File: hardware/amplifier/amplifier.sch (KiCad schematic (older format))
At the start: 39 parts, among them IC3 AD8331, IC4 ISL55210, P2 OUT, X1 IN

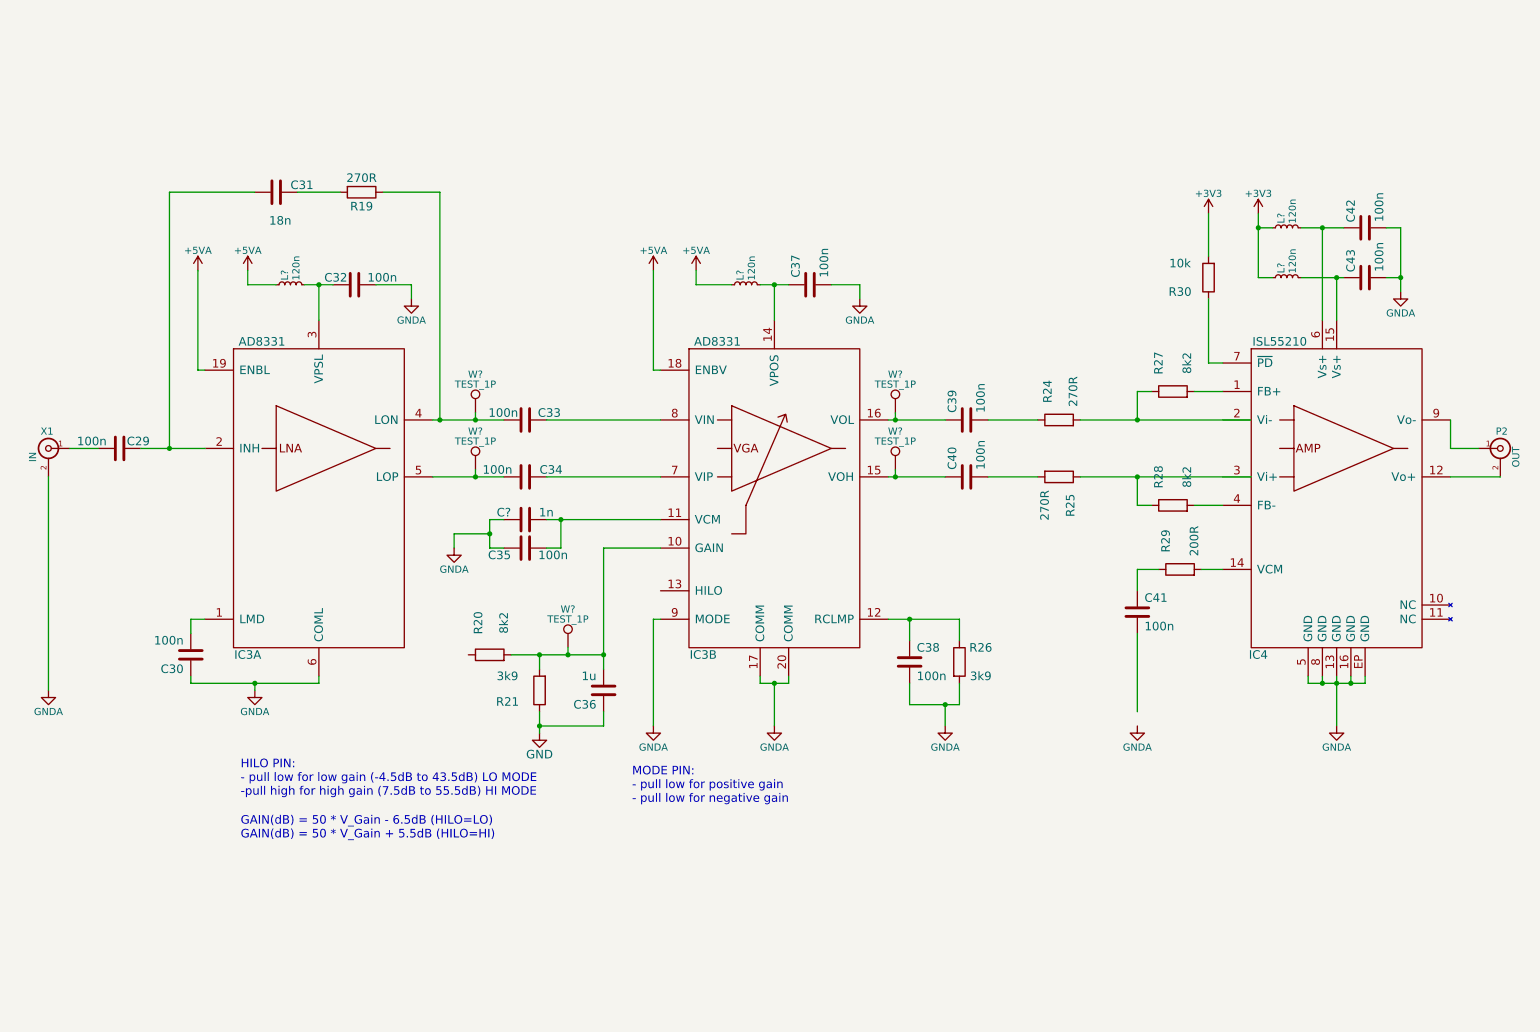
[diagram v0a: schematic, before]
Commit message: Worked on amp schema; nearly done; ISL55210 needs review as well as output termination
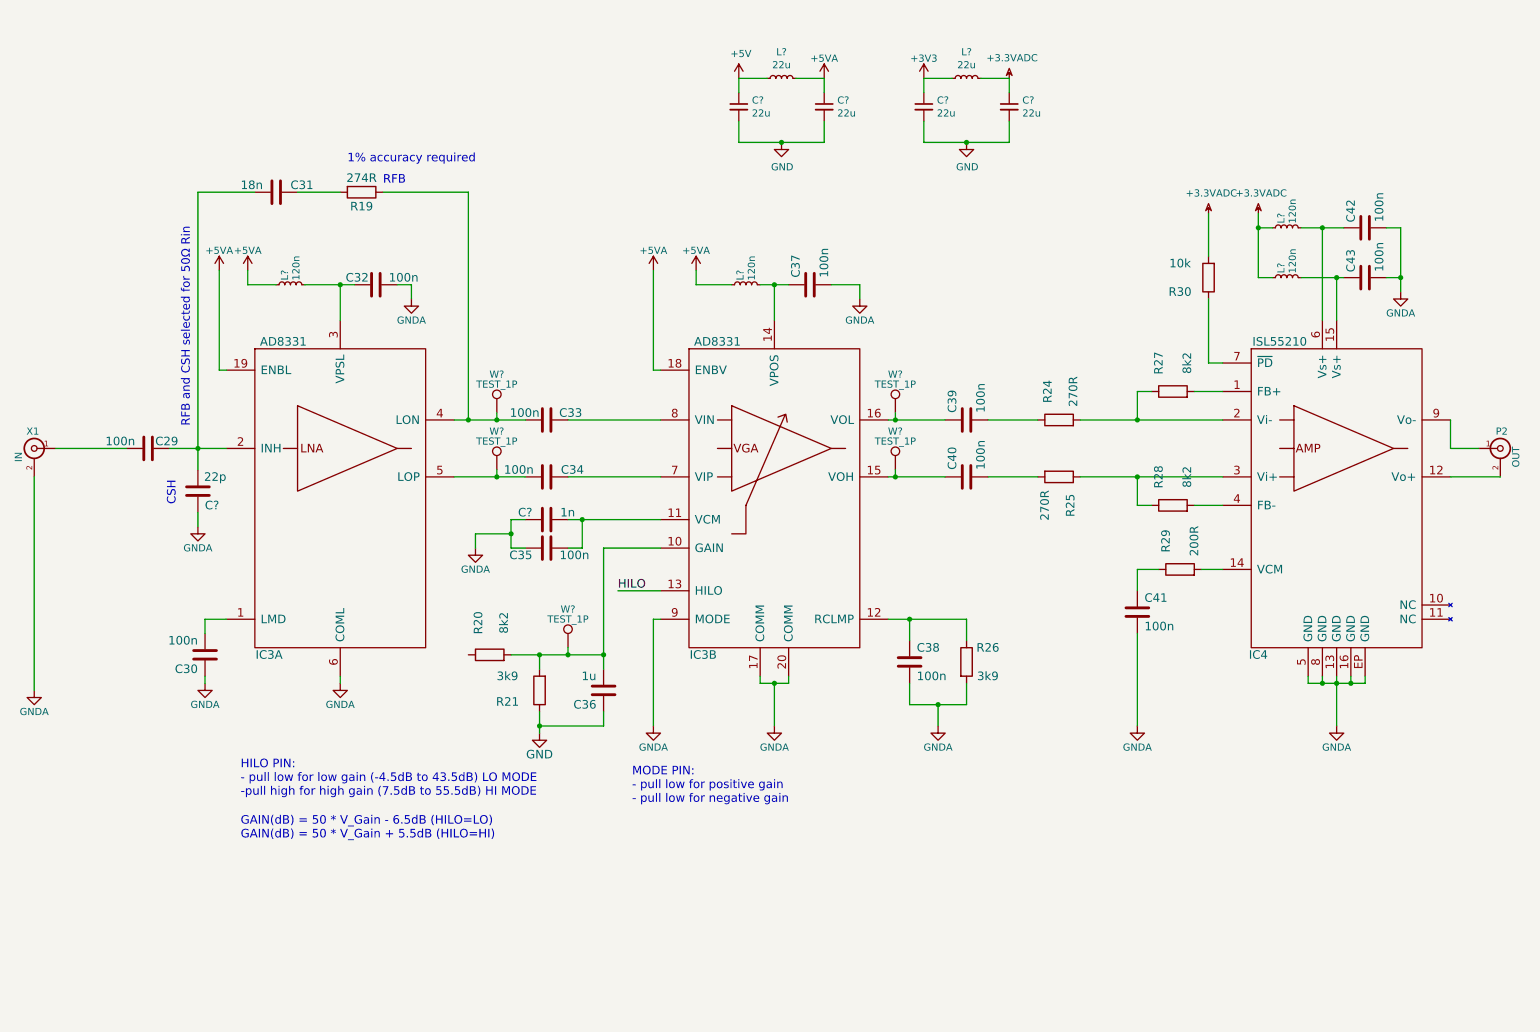
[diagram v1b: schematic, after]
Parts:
- added C? (x4): 22u, symbol C_Small
- added C?: 22p, SDR:0603, symbol C
- added L? (x2): 22u, symbol L_Small
- R19: value 270R -> 274R
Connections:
- net +3V3: now also C?.1, L?.1; no longer L?.1, L?.1, R30.2
- net +5VA: now also C?.1, L?.2
- net GND: now also C?.2, C?.2, C?.2, C?.2
- net GNDA: now also C41.2, C?.1
- net at C29.1, C31.2, IC3.2 (INH): now also C?.2
- net HILO: now reaches IC3.13 (HILO)
- net at IC4.2 (Vi-): now also R24.2, R27.1
- net at IC4.3 (Vi+): now also R25.1, R28.1
- new net +3.3VADC: C?.1, L?.1, L?.1, L?.2, R30.2
- new net +5V: C?.1, L?.1
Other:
- note added: "1% accuracy required"
- note added: "CSH"
- note added: "RFB"
- note added: "RFB and CSH selected for 50Ω Rin"
- moved on the sheet: C29, C30, C32, C33, C34, C35, C?, IC3A, R26, W?, X1

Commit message: schema done for now; needs some minor changes; routing done for this schema
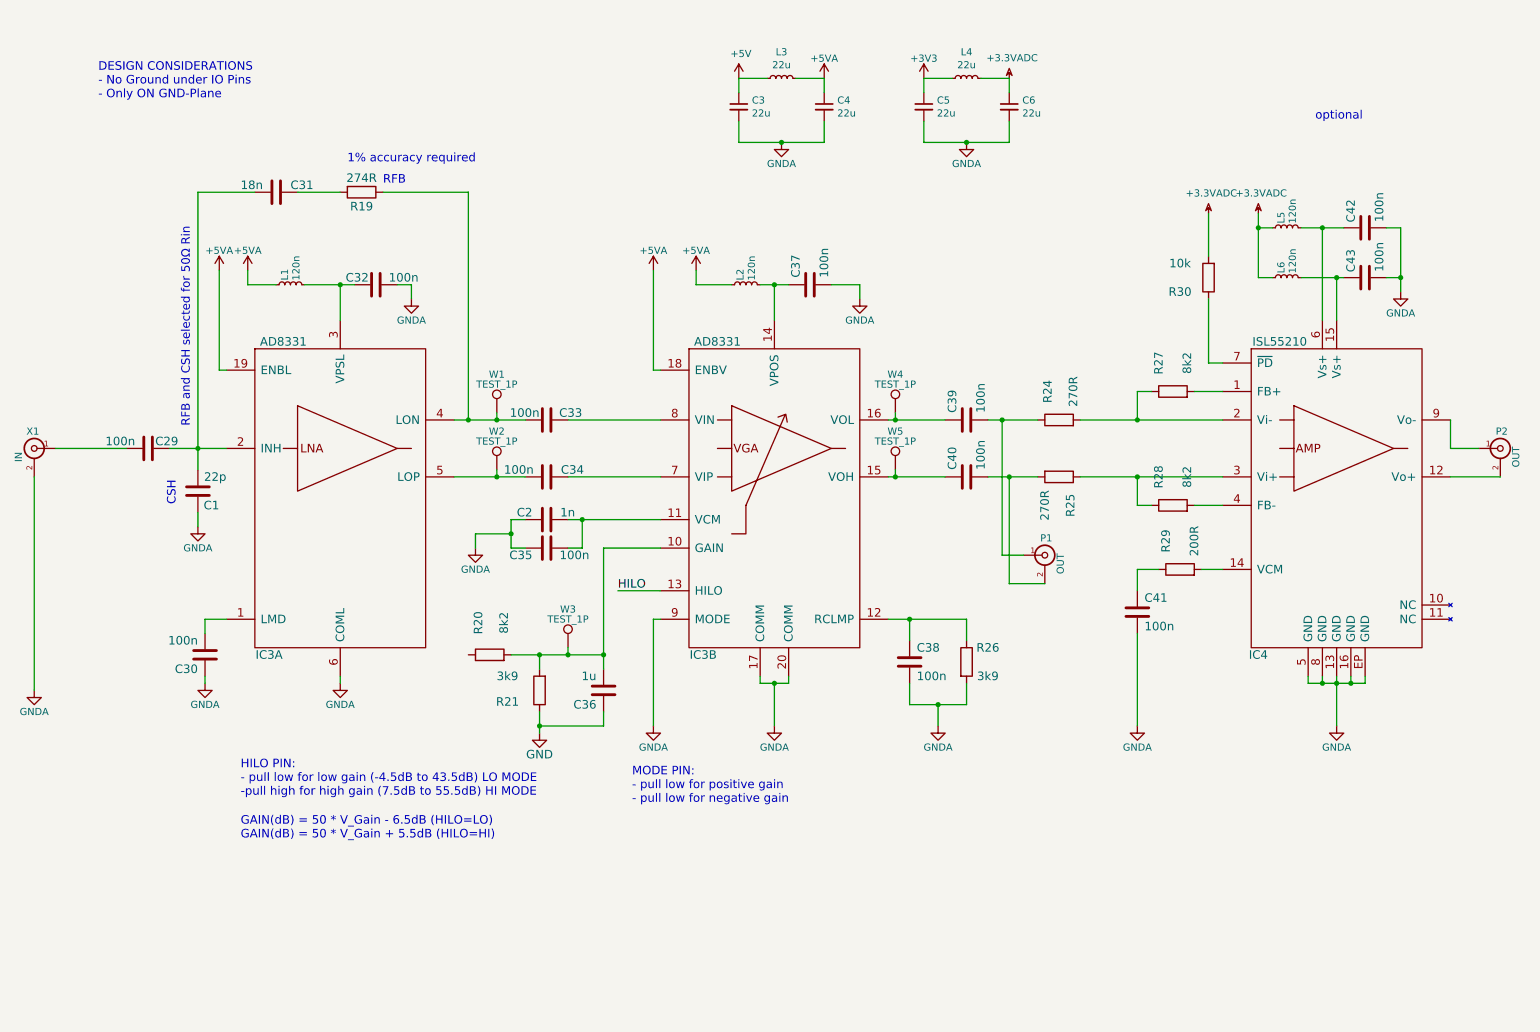
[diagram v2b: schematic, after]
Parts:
- added P1: OUT, SDRfootprints:1-1337543-0, symbol BNC
- C1, C2: renamed from C?; footprint SDR:0603 -> Capacitors_SMD:C_0603
- C29, C30, C31, C32, C33, C34, C35, C36, C37, C38, C39, C40, C41, C42, C43: footprint SDR:0603 -> Capacitors_SMD:C_0603
- C3, C4, C5, C6: renamed from C?; footprint (none) -> Capacitors_SMD:C_1210
- IC3: footprint SDR:QSOP20 -> SDRfootprints:QSOP20
- IC4: footprint SDR:TQFN16 -> SDRfootprints:TQFN16
- L1, L2, L5, L6: renamed from L?; footprint (none) -> Resistors_SMD:R_0603
- L3, L4: renamed from L?; footprint (none) -> SDRfootprints:COIL_445-4177-1-ND
- R19, R20, R21, R24, R25, R26, R27, R28, R29, R30: footprint SDR:0603 -> Resistors_SMD:R_0603
- W1, W2, W3, W4, W5: renamed from W?; footprint (none) -> Measurement_Points:Test_Point_Keystone_5005-5009_Compact
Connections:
- net GND: no longer C3.2, C4.2, C5.2, C6.2
- net GNDA: now also C3.2, C4.2, C5.2, C6.2
- net at C40.2, R25.2: now also P1.2 (Ext)
- net at C39.2, R24.1: now also P1.1 (In)
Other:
- note added: "DESIGN CONSIDERATIONS\n- No Ground under IO Pins\n- Only ON GND-Plane"
- note added: "optional\n"

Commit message: amp done
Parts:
- removed R20: 8k2, Resistors_SMD:R_0603, symbol R
- removed R21: 3k9, Resistors_SMD:R_0603, symbol R
- added C11, C4: 100n, Capacitors_SMD:C_0603, symbol C
- added R1: 330k, Resistors_SMD:R_0603, symbol R
- added R2: 82k, Resistors_SMD:R_0603, symbol R
- added U1: MCP4706/16/26, TO_SOT_Packages_SMD:SOT-23-6, symbol MCP4706/16/26
- X2: renamed from P1; value OUT -> OUT_1
- X3: renamed from P2; value OUT -> OUT_2
- renumbered C29 to C1, C35 to C10, C36 to C12, C3 to C13, C37 to C14, C4 to C15, C38 to C16, C5 to C17, C39 to C18, C40 to C19, C1 to C2, C6 to C20, C41 to C21, C42 to C22, C43 to C23, C30 to C3, C31 to C5, C32 to C6, C33 to C7, C34 to C8, C2 to C9, IC3 to IC1, IC4 to IC2, R30 to R10, R19 to R3, R26 to R4, R24 to R5, R25 to R6, R27 to R7, R28 to R8, R29 to R9
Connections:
- net GND is gone; now on net GNDA: C12.1
- net +5VA: now also C11.1, R1.1, U1.3 (VDD)
- net GNDA: now also C11.2, C4.2, R2.2, U1.2 (VSS)
- net at C12.2, IC1.10 (GAIN), W3.1: now also U1.1 (VOUT)
- new net: C4.1, R1.2, R2.1, U1.6 (VREF)
- new net SCL: U1.5 (SCL)
- new net SDA: U1.4 (SDA)
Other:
- note added: "ferrite bead"
- moved on the sheet: C1, C10, C12, C13, C14, C15, C16, C17, C18, C19, C2, C20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

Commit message: Amp PCB completely done with power taps and baluns
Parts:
- added C24, C25: TBD, Capacitors_SMD:C_0603, symbol C
- added J1: 0, Resistors_SMD:R_0603, symbol R
- added P1: 5V, Pin_Headers:Pin_Header_Angled_1x02, symbol CONN_01X02
- added P2: 3V3, Pin_Headers:Pin_Header_Angled_1x02, symbol CONN_01X02
- added P3: Interface, Pin_Headers:Pin_Header_Angled_1x03, symbol CONN_01X03
- added R14, R5, R6: TBD, Resistors_SMD:R_0603, symbol R
- added R15, R16, R9: 10k, Resistors_SMD:R_0603, symbol R
- added T1, T2: BALUN, SDRfootprints:CX2041NLT, symbol TRANSFO4
- R12: renamed from R9; value 200R -> 200
- R13: renamed from R10; value 10k -> TBD
- R3: value 274R -> 274
- R7: renamed from R5; value 270R -> 270
- R8: renamed from R6; value 270R -> 270
- renumbered R7 to R10, R8 to R11
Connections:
- net +3.3VADC: now also R9.1; no longer R13.2
- net +3V3: now also P2.2 (P2)
- net +5V: now also P1.2 (P2)
- net +5VA: now also R15.1, R16.1
- net GNDA: now also X2.2 (Ext), X3.2 (Ext), C24.1, C25.2, P1.1 (P1), P2.1 (P1), T1.2 (PM), T2.2 (PM)
- net HILO: now also P3.1 (P1)
- net SCL: now also P3.2 (P2), R16.2
- net SDA: now also P3.3 (P3), R15.2
- net at C12.2, IC1.10 (GAIN), W3.1: now also J1.1; no longer U1.1 (VOUT)
- net at IC2.12 (Vo+): now also R14.1; no longer X3.2 (Ext)
- net at IC2.7 (~PD): now also R9.2; no longer R13.1
- net at IC2.9 (Vo-): now also R13.1; no longer X3.1 (In)
- net at C19.2, R8.2: now also R6.1; no longer X2.2 (Ext)
- net at C18.2, R7.1: now also R5.1; no longer X2.1 (In)
- new net: T2.1 (PR1), T2.3 (PR2), X3.1 (In)
- new net: T1.1 (PR1), T1.3 (PR2), X2.1 (In)
- new net: J1.2, U1.1 (VOUT)
- new net OUT1+: C25.1, R14.2, T1.5 (S2)
- new net OUT1-: C24.2, R13.2, T1.4 (S1)
- new net OUT2+: R6.2, T2.4 (S1)
- new net OUT2-: R5.2, T2.5 (S2)
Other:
- note removed: "optional\n"
- moved on the sheet: C1, C10, C11, C12, C13, C14, C15, C16, C17, C18, C19, C2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
